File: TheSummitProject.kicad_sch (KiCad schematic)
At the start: 35 parts, among them IC1 STM32U5F7VJT6, J1 Cortex SWD, SW1 SW_SPDT, U2 USBLC6-2SC6, U3 USBLC6-2SC6, Y1 16Mhz, Y2 32.768Khz

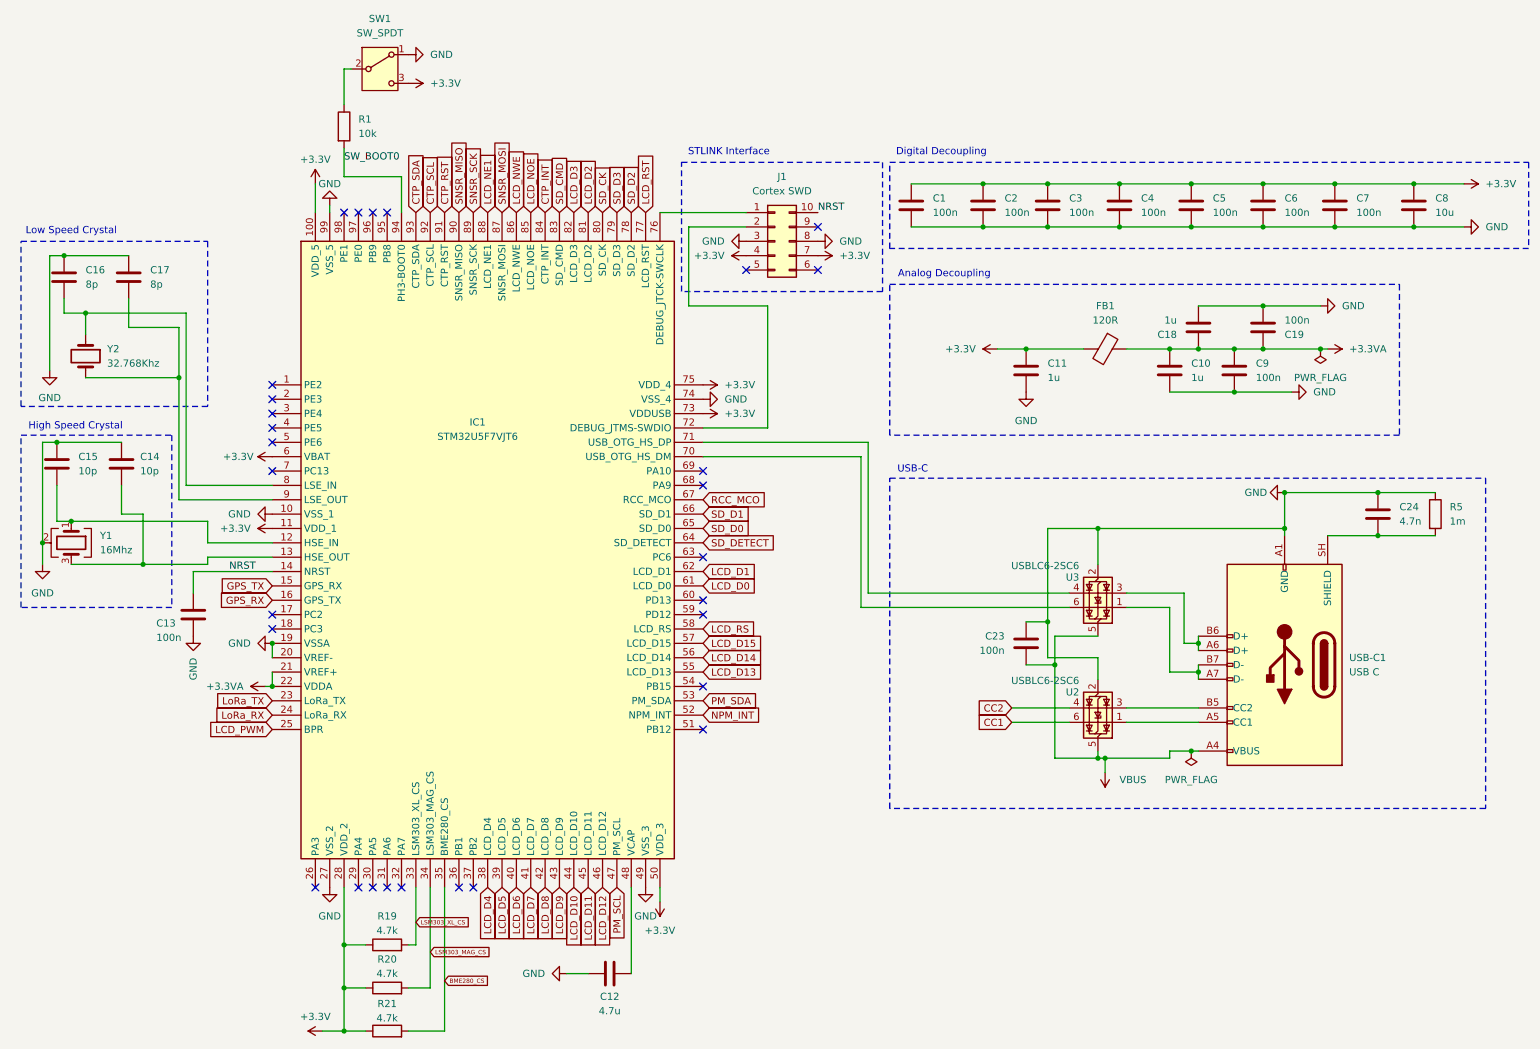
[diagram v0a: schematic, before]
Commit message: Updated with new power rails, added sensors and gps symbol
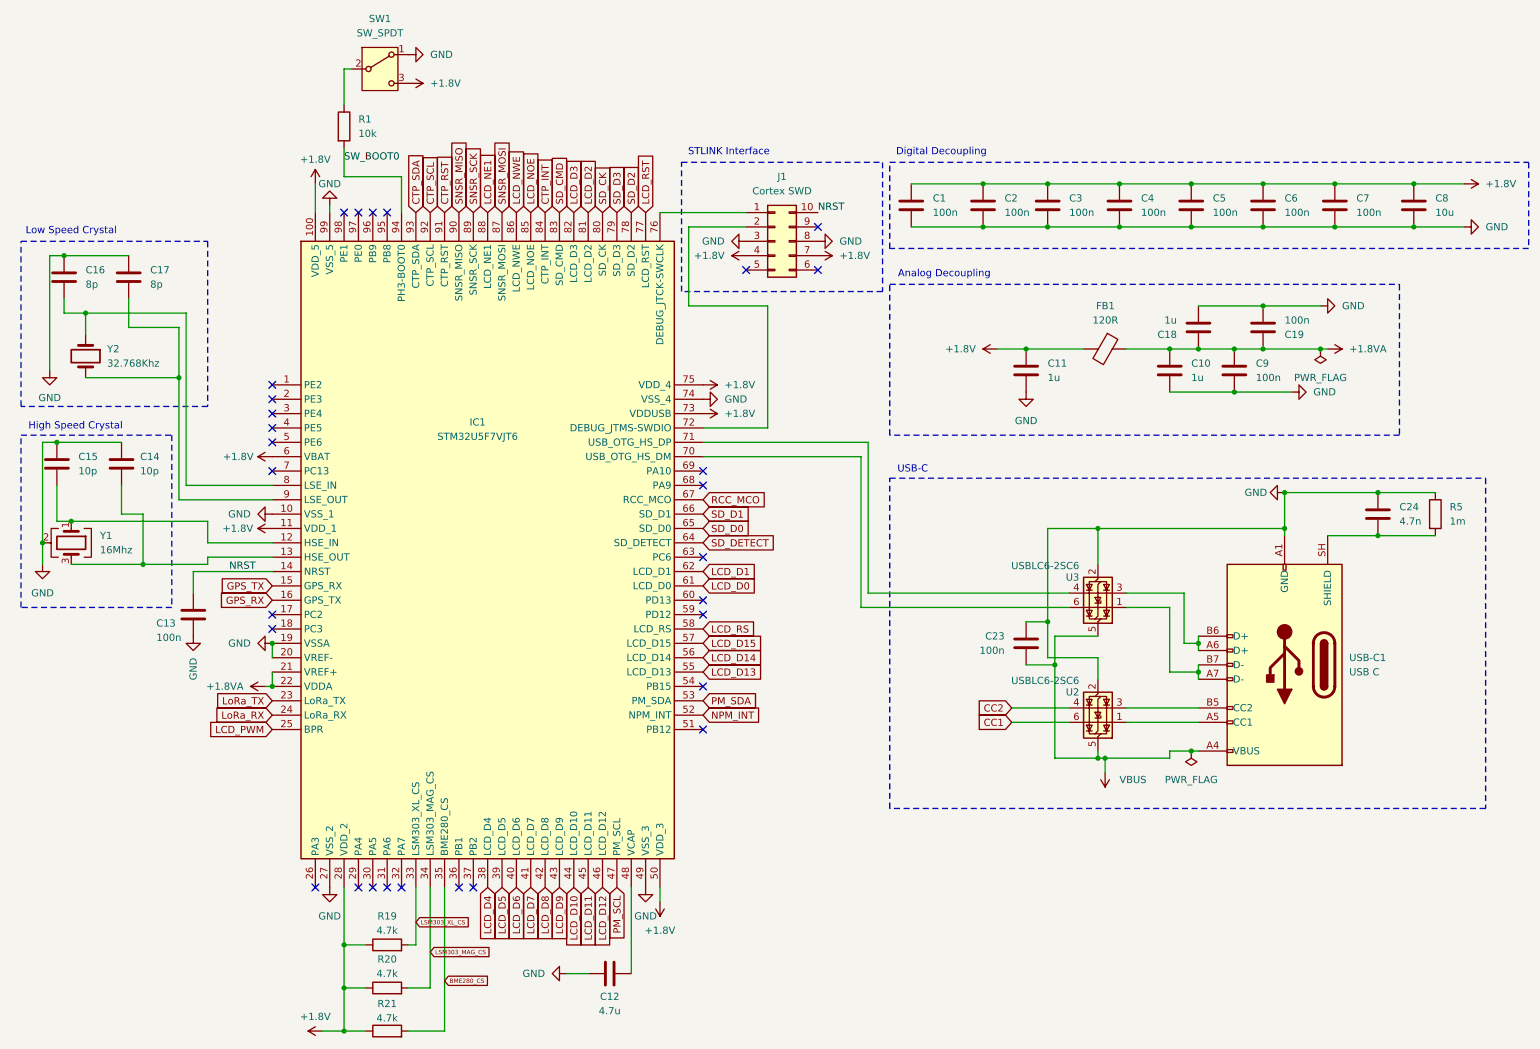
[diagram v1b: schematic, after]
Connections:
- net +3.3V renamed +1.8V
- net +3.3VA renamed +1.8VA
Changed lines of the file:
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@@
 			)
 		)
-		(property "Value" "+3.3V"
+		(property "Value" "+1.8V"
 			(at 139.7 58.4199 90)
 			(show_name no)
@@
 			)
 		)
-		(property "Value" "+3.3V"
+		(property "Value" "+1.8V"
 			(at 128.27 177.8 0)
 			(show_name no)
@@
 			)
 		)
-		(property "Value" "+3.3V"
+		(property "Value" "+1.8V"
 			(at 274.32 45.7199 90)
 			(show_name no)
@@
 			)
 		)
-		(property "Value" "+3.3VA"
+		(property "Value" "+1.8VA"
 			(at 250.19 74.9299 90)
 			(show_name no)
@@
 			)
 		)
-		(property "Value" "+3.3V"
+		(property "Value" "+1.8V"
 			(at 139.7 86.3599 90)
 			(show_name no)
@@
 			)
 		)
-		(property "Value" "+3.3V"
+		(property "Value" "+1.8V"
 			(at 67.31 41.402 0)
 			(show_name no)
@@
 			)
 		)
-		(property "Value" "+3.3V"
+		(property "Value" "+1.8V"
 			(at 87.63 27.9399 90)
 			(show_name no)
@@
 		(in_pos_files yes)
 		(dnp no)
-		(fields_autoplaced yes)
 		(property "Reference" "#PWR09"
 			(at 63.5 106.68 0)
@@
 			)
 		)
-		(property "Value" "+3.3V"
-			(at 55.88 106.6799 90)
+		(property "Value" "+1.8V"
+			(at 53.594 106.68 90)
 			(show_name no)
 			(do_not_autoplace no)
@@
 					(size 1.27 1.27)
 				)
-				(justify left)
 			)
 		)
@@
 			)
 		)
-		(property "Value" "+3.3V"
+		(property "Value" "+1.8V"
 			(at 67.31 193.04 90)
 			(show_name no)
@@
 			)
 		)
-		(property "Value" "+3.3V"
+		(property "Value" "+1.8V"
 			(at 184.15 74.9299 90)
 			(show_name no)
@@
 			)
 		)
-		(property "Value" "+3.3V"
+		(property "Value" "+1.8V"
 			(at 160.02 58.4199 90)
 			(show_name no)
@@
 			)
 		)
-		(property "Value" "+3.3V"
+		(property "Value" "+1.8V"
 			(at 139.7 81.2799 90)
 			(show_name no)
@@
 			)
 		)
-		(property "Value" "+3.3VA"
+		(property "Value" "+1.8VA"
 			(at 54.61 134.6199 90)
 			(show_name no)
@@
 			)
 		)
-		(property "Value" "+3.3V"
+		(property "Value" "+1.8V"
 			(at 56.388 93.98 90)
 			(show_name no)

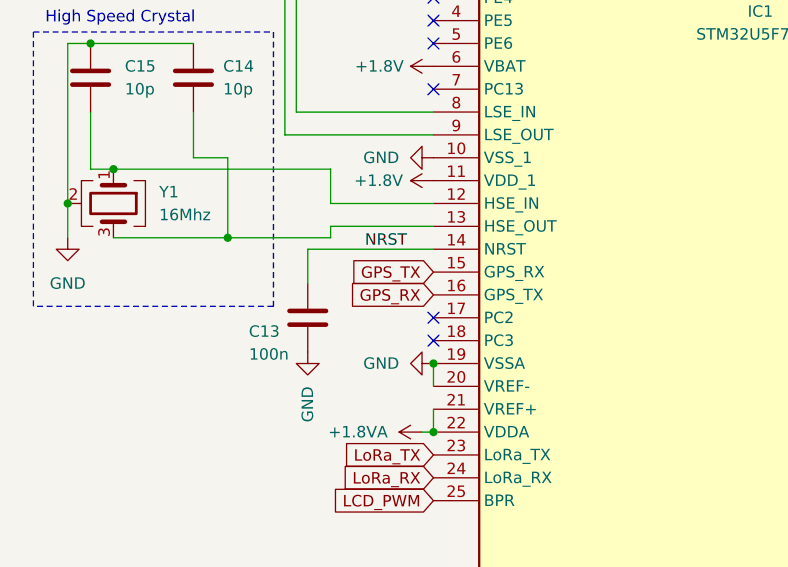
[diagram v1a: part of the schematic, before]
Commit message: Added logic level shifter for lora
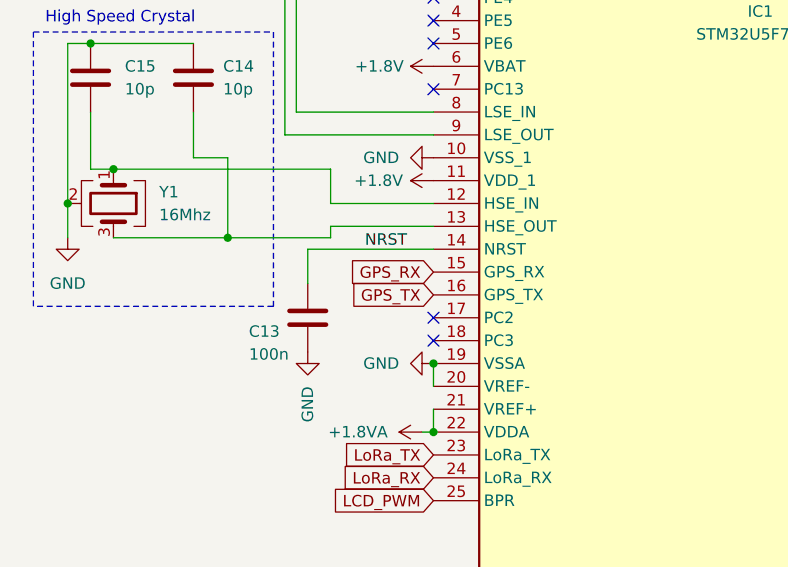
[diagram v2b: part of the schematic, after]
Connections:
- net GPS_RX: now also IC1.15 (GPS_RX); no longer IC1.16 (GPS_TX)
- net GPS_TX: now also IC1.16 (GPS_TX); no longer IC1.15 (GPS_RX)
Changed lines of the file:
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@@
 	(global_label "GPS_TX"
 		(shape input)
-		(at 59.69 116.84 180)
+		(at 59.69 119.38 180)
 		(fields_autoplaced yes)
 		(effects
@@
 		)
 		(property "Intersheetrefs" "${INTERSHEET_REFS}"
-			(at 49.8106 116.84 0)
+			(at 49.8106 119.38 0)
 			(hide yes)
 			(show_name no)
@@
 	(global_label "GPS_RX"
 		(shape input)
-		(at 59.69 119.38 180)
+		(at 59.69 116.84 180)
 		(fields_autoplaced yes)
 		(effects
@@
 		)
 		(property "Intersheetrefs" "${INTERSHEET_REFS}"
-			(at 49.5082 119.38 0)
+			(at 49.5082 116.84 0)
 			(hide yes)
 			(show_name no)

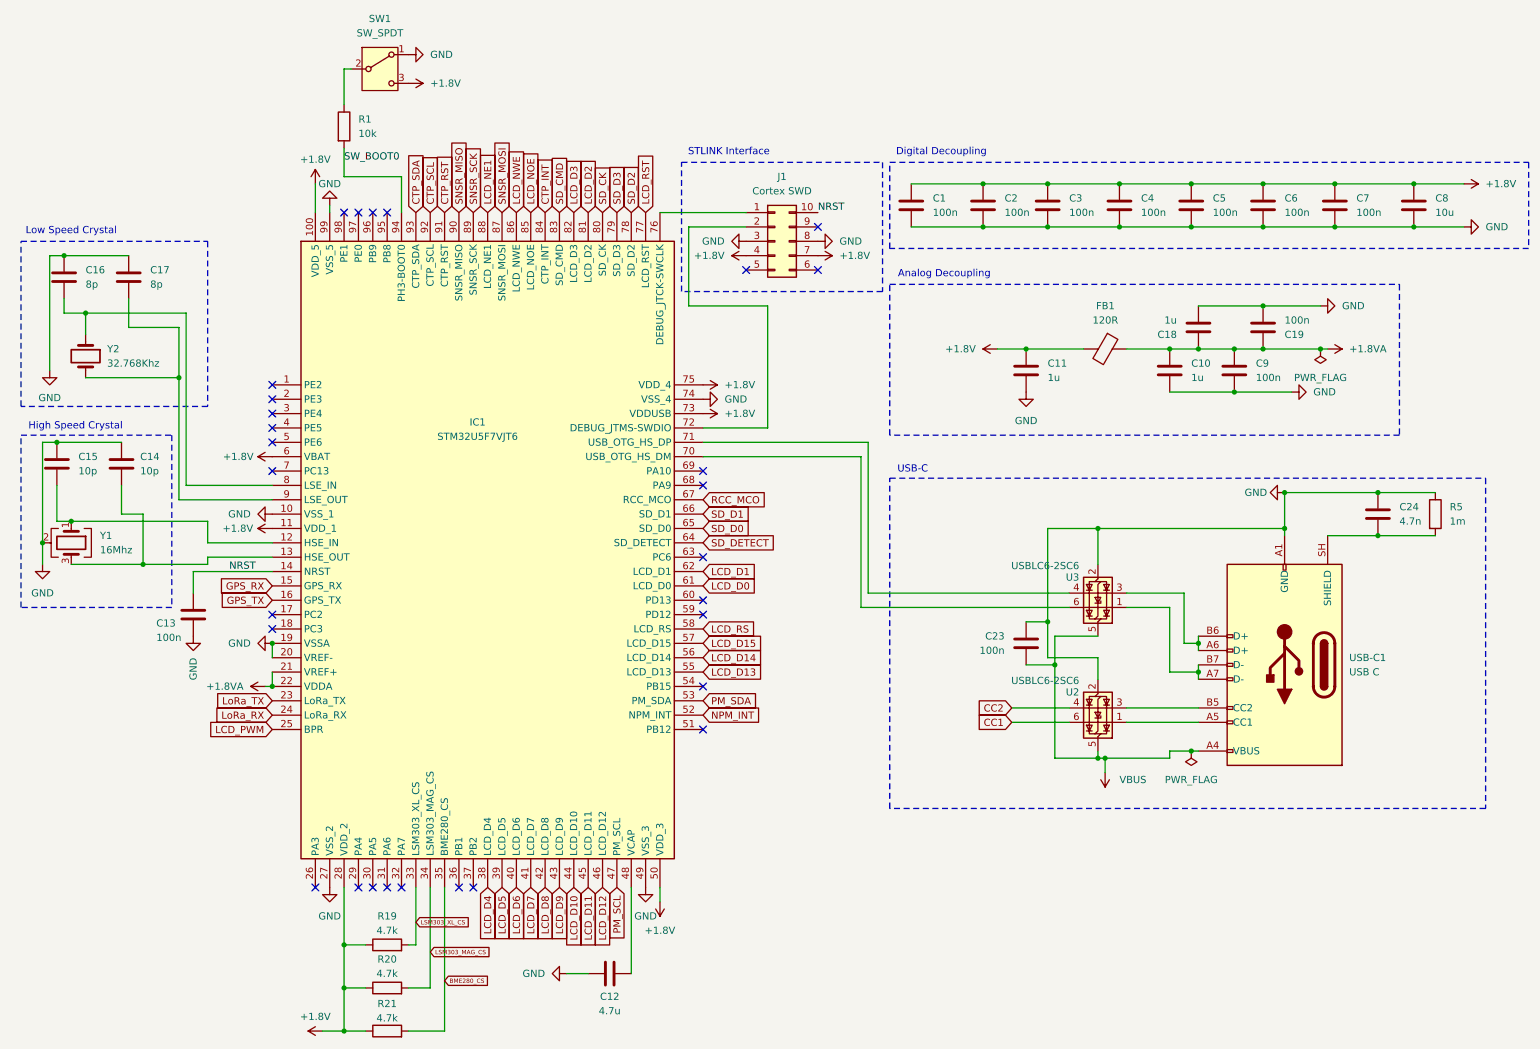
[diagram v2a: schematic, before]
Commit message: added mux for usb, cleaned up schematic for pcb design, setup new pcb with correct size
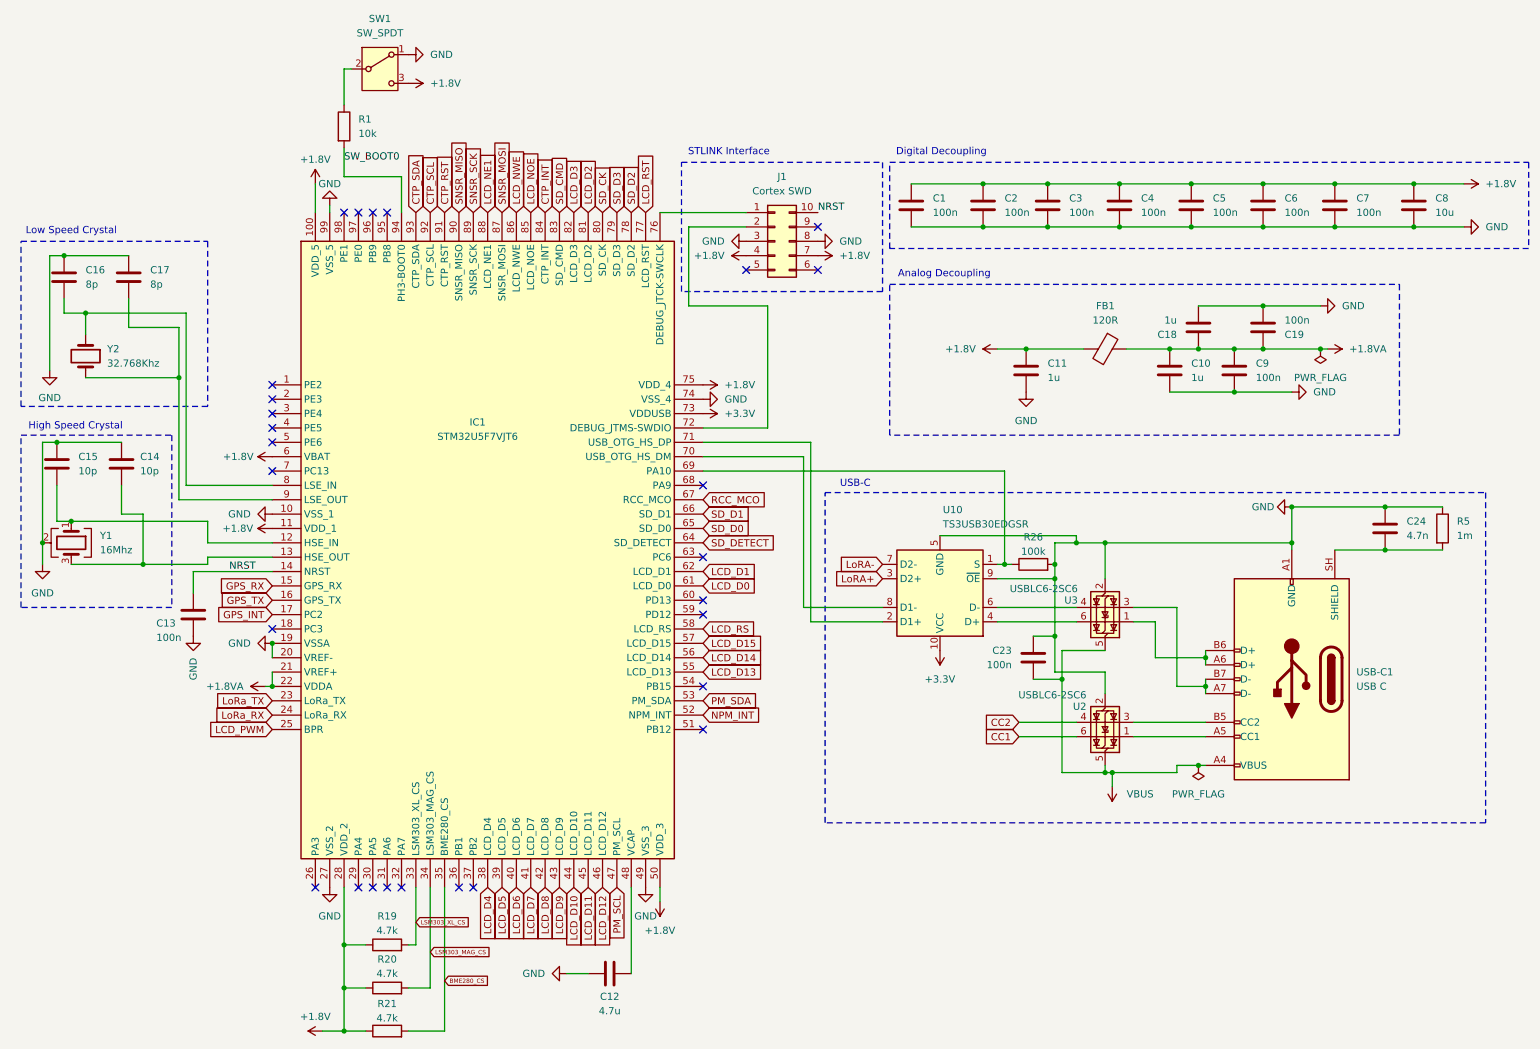
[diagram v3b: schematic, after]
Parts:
- added R26: 100k, Resistor_SMD:R_0603_1608Metric, symbol Device:R
- added U10: TS3USB30EDGSR, Package_SO:TSSOP-10_3x3mm_P0.5mm, symbol Interface_USB:TS3USB30EDGSR
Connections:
- net +1.8V: no longer IC1.73 (VDDUSB)
- net GND: now also R26.2, U10.5 (GND), U10.9 (~{OE})
- net at USB-C1.A7 (D-), USB-C1.B7 (D-): now also U3.3 (I/O2); no longer U3.1 (I/O1)
- net at USB-C1.A6 (D+), USB-C1.B6 (D+): now also U3.1 (I/O1); no longer U3.3 (I/O2)
- net at U3.4 (I/O2): now also U10.6 (D-); no longer IC1.71 (USB_OTG_HS_DP)
- net at U3.6 (I/O1): now also U10.4 (D+); no longer IC1.70 (USB_OTG_HS_DM)
- net GPS_INT: now reaches IC1.17 (PC2)
- net at IC1.69 (PA10): now also R26.1, U10.1 (S)
- new net: IC1.70 (USB_OTG_HS_DM), U10.8 (D1-)
- new net: IC1.71 (USB_OTG_HS_DP), U10.2 (D1+)
- new net +3.3V: IC1.73 (VDDUSB), U10.10 (VCC)
- new net LoRA+: U10.3 (D2+)
- new net LoRA-: U10.7 (D2-)
- no-connect marks 29 -> 27
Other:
- moved on the sheet: C23, C24, R5, U2, U3, USB-C1

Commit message: Changed SPI to 3-wire, added Accelerometer interupt
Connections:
- net SNSR_MISO renamed ACC_INT
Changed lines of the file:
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@@
 		)
 	)
-	(global_label "SNSR_MISO"
+	(global_label "ACC_INT"
 		(shape input)
 		(at 92.71 50.8 90)
@@
 		)
 		(property "Intersheetrefs" "${INTERSHEET_REFS}"
-			(at 92.71 37.2315 90)
+			(at 92.71 40.3157 90)
 			(hide yes)
 			(show_name no)

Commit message: pcb draft, cleaned up schematic
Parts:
- removed C10, C11, C18: 1u, Capacitor_SMD:C_0603_1608Metric, symbol Device:C
- removed C6, C7: 100n, Capacitor_SMD:C_0603_1608Metric, symbol Device:C
- removed FB1: 120R, Inductor_SMD:L_0603_1608Metric, symbol Device:FerriteBead
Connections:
- net +1.8V: now also C19.1, C9.2, IC1.21 (VREF+), IC1.22 (VDDA)
- net GND: now also C9.1; no longer C9.2
- net PIEZO_P1: now reaches IC1.2 (PIEZO_P1)
- net PIEZO_P2: now reaches IC1.3 (PIEZO_P2)
- removed net +1.8VA: C19.1, C9.1, IC1.21 (VREF+), IC1.22 (VDDA)
- net LCD_D10: no longer names the net of IC1.44 (LCD_D10)
- net LCD_D11: no longer names the net of IC1.45 (LCD_D11)
- net LCD_D12: no longer names the net of IC1.46 (LCD_D12)
- net LCD_D13: no longer names the net of IC1.55 (LCD_D13)
- net LCD_D14: no longer names the net of IC1.56 (LCD_D14)
- net LCD_D15: no longer names the net of IC1.57 (LCD_D15)
- net LCD_D8: no longer names the net of IC1.42 (LCD_D8)
- net LCD_D9: no longer names the net of IC1.43 (LCD_D9)
- no-connect marks 27 -> 33
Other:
- moved on the sheet: C8
